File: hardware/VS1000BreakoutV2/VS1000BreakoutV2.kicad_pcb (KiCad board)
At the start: 2 copper layers, 55.9 x 24.9 mm, 27 parts, among them J1 Power Jumper, J2 Conn_01x14_Male, J3 USB_B_Micro, J4 Conn_01x14_Male, J5 AudioJack4, U1 VS1000, U2 USBLC6-2SC6, U3 MX25L6473FM2I-08G, Y1 12MHz

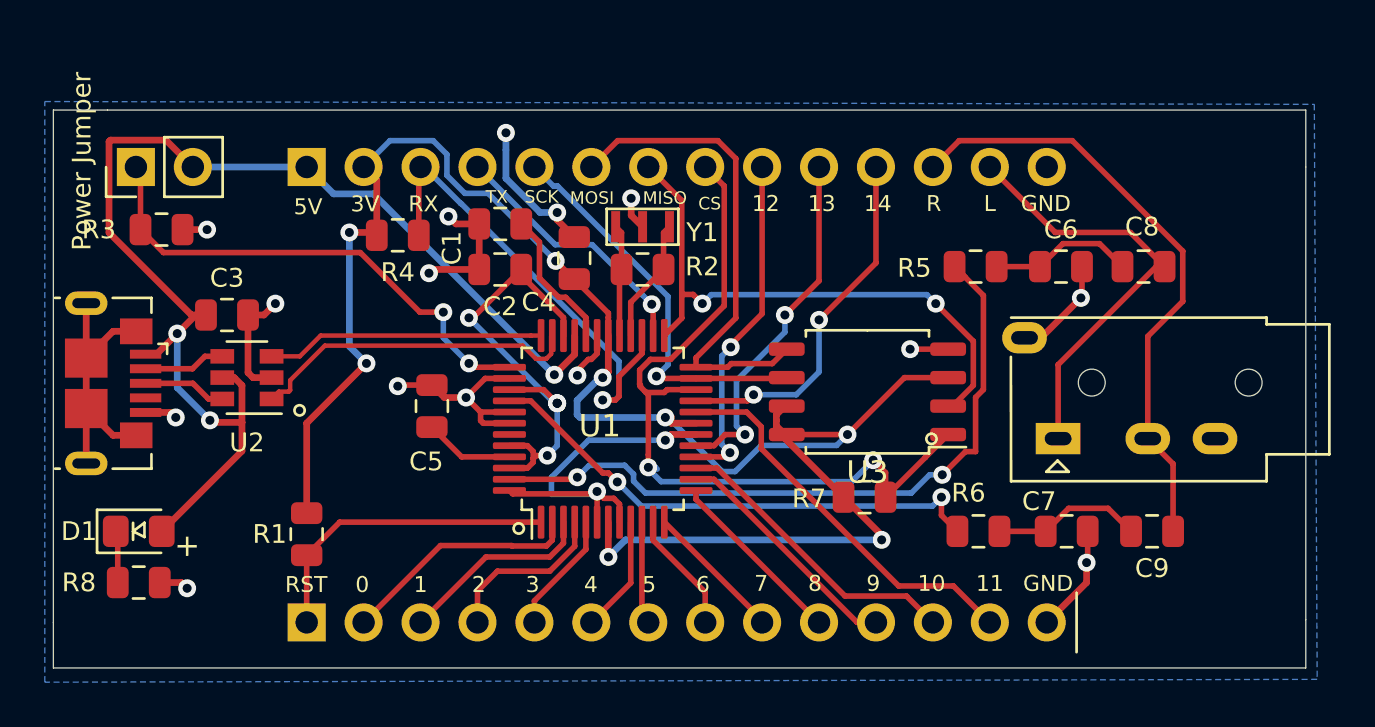
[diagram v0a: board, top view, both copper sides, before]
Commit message: vs1000 breakout PCB updates
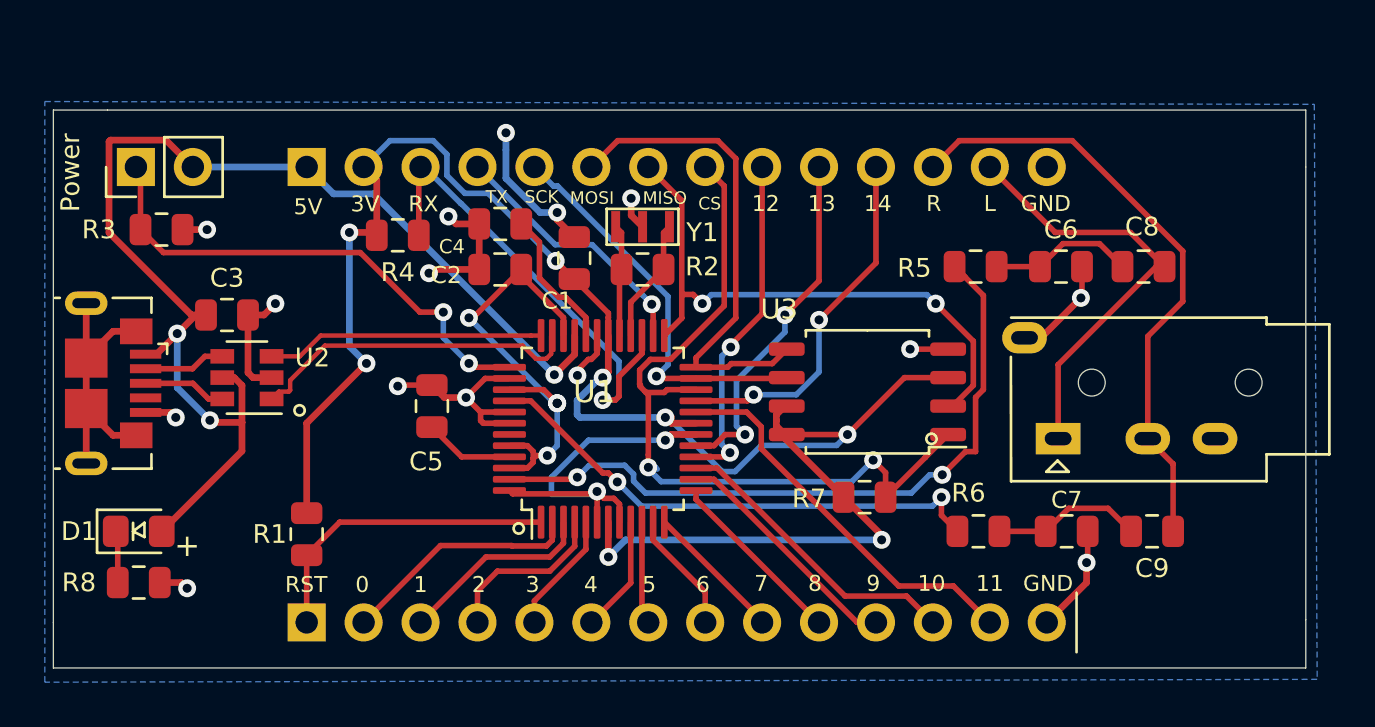
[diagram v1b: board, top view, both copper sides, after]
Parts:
-  : renamed from J1; value Power Jumper -> Power
- J2, J4: value Conn_01x14_Male -> (none)
- U2: value USBLC6-2SC6 -> USBLC6
- U3: value MX25L6473FM2I-08G -> MX25L
